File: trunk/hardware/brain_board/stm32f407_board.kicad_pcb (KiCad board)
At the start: 2 copper layers, 65.8 x 73.2 mm, 63 parts, among them J1 MINI-USB-5P-3400020P1, P1 CONN_25X2, P2 CONN_25X2, P3 CONN_2, P4 CONN_6, SW1 SW_PUSH, SW2 SW_PUSH, U1 STM32F407VG, U2 USBUF02W6, U3 LM2937, X1 CRYSTAL

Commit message: improved version
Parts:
- moved C1 14.2 mm to (130.6, 121.9), turned to 270 degrees
- moved C10 11.0 mm to (101.2, 95.0), turned to 180 degrees
- moved C9 8.27 mm to (128.5, 93.6)
- moved R11 5.69 mm to (120.8, 87.1), turned to 90 degrees
- moved C7 5.62 mm to (104.0, 101.1)
- moved D6 5.59 mm to (132.2, 148.7)
- moved FB1 5.36 mm to (101.1, 96.9)
- moved C11 4.95 mm to (112.1, 95.5)
- moved R3 4.13 mm to (120.1, 132.7), turned to 0 degrees
- moved R12 3.78 mm to (129.2, 149.5), turned to 90 degrees
- moved R10 3.72 mm to (104.9, 103.8)
- moved R4 3.32 mm to (132.2, 107.6)
- moved R1 3.28 mm to (117.0, 126.0), turned to 0 degrees
- moved C15 3.14 mm to (106.9, 121.8)
- moved R14 2.92 mm to (126.2, 154.8)
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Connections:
- C7 pad 2: N-0000046 -> N-00000118
- C8 pad 2: N-00000119 -> N-00000118
- FB1 pad 1: N-0000046 -> N-00000118
- R10 pad 1: N-0000046 -> N-00000118
- U1 pad 22: N-0000046 -> N-00000118
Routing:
- net GND: track 122.7 -> 421.1 mm, vias 28 -> 21
- net /VDD: track 323.6 -> 260.4 mm, vias 4 -> 7
- net /PA13: track 149.9 -> 91.8 mm, vias 0 -> 1
- net /PA14: track 134.9 -> 88.4 mm, vias 0 -> 2
- net /NRST: track 89.2 -> 114.5 mm
- net N-00000118: track 0.00 -> 21.2 mm
- net N-0000045: track 67.8 -> 49.1 mm
- net /PA12: track 25.6 -> 44.1 mm
- net /PE6: track 39.7 -> 22.6 mm
- net /PC9: track 43.3 -> 58.6 mm
- net /BOOT0: track 21.2 -> 35.9 mm, vias 0 -> 1
- net /PC7: track 46.9 -> 60.5 mm
- net /PD14: track 44.8 -> 57.5 mm
- net N-0000046: track 12.0 -> 0.00 mm
- net N-0000017: track 23.6 -> 13.1 mm
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
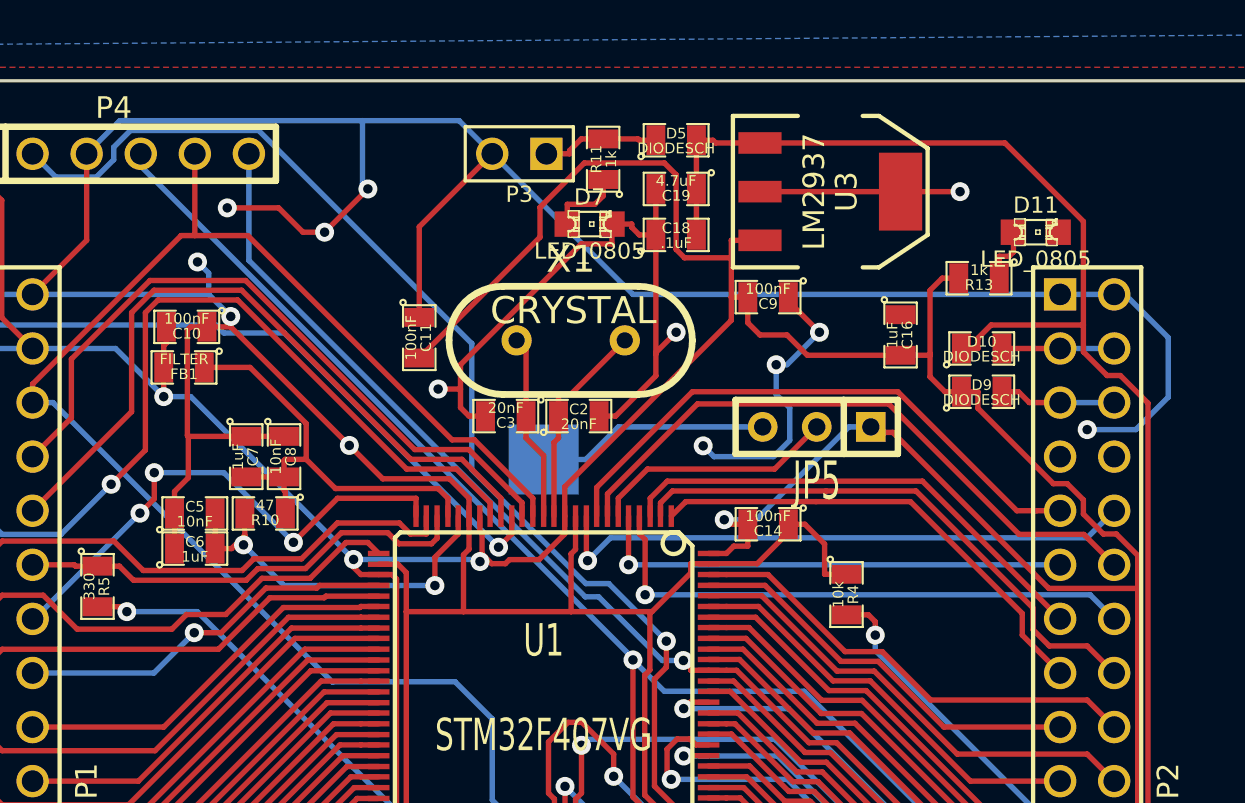
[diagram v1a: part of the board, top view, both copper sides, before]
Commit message: with RTC crystal
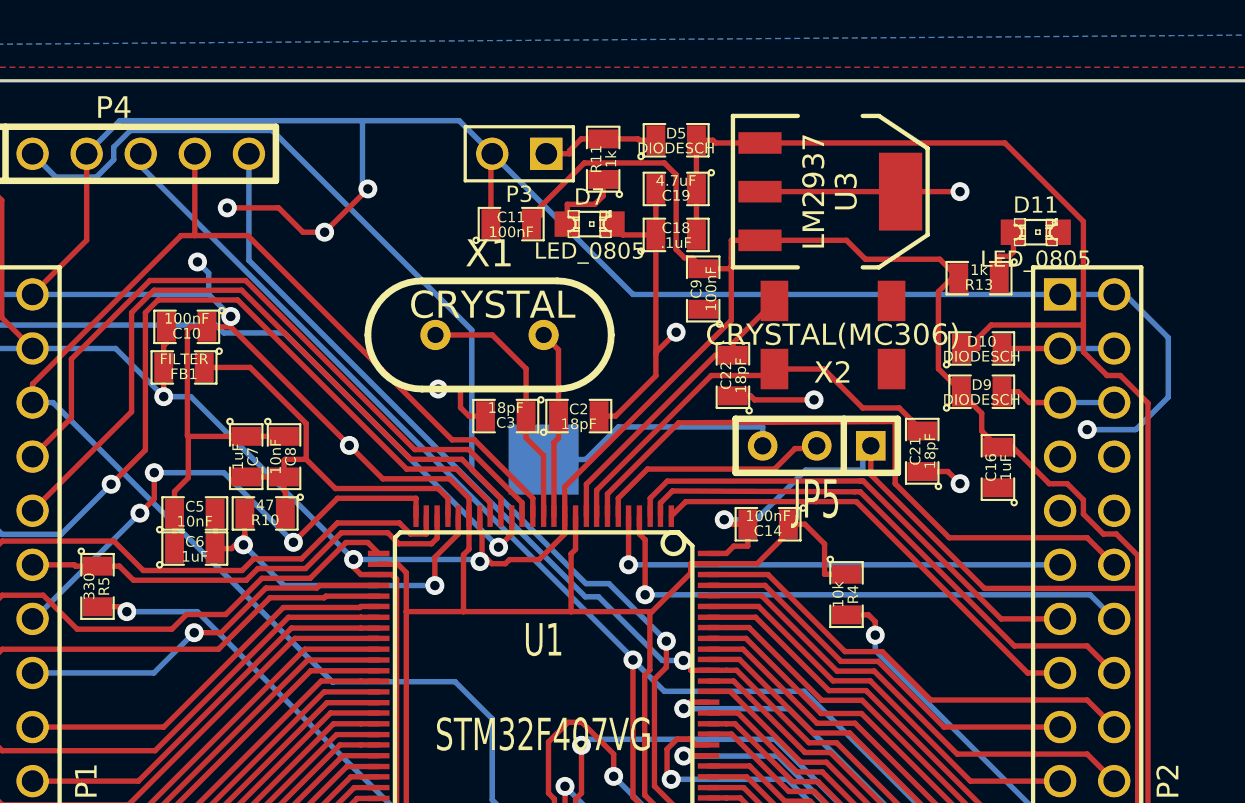
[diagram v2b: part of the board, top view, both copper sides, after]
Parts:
- added C21: 18pF, SM0805, F.Cu at (135.8, 100.8)
- added C22: 18pF, SM0805, F.Cu at (126.9, 97.3)
- added X2: CRYSTAL(MC306), MC-306, F.Cu at (131.6, 95.4)
- C2, C3: value 20nF -> 18pF
- moved C16 7.72 mm to (139.3, 101.6), turned to 90 degrees
- moved C11 6.86 mm to (116.5, 90.2), turned to 0 degrees
- moved X1 3.82 mm to (115.4, 95.4)
- moved C9 3.07 mm to (125.5, 93.2), turned to 90 degrees
- moved JP5 0.89 mm to (130.8, 100.6)
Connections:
- P2 pad 10: /PC15 -> N-0000075
- P2 pad 9: /PC14 -> N-0000076
- U1 pad 8: /PC14 -> N-0000073
- U1 pad 9: /PC15 -> N-0000074
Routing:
- net /PC15: track 27.8 -> 0.00 mm, vias 1 -> 0
- net /PC14: track 27.3 -> 0.00 mm
- net GND: track 421.1 -> 396.2 mm, vias 21 -> 20
- net N-0000073: track 0.00 -> 20.1 mm
- net N-0000074: track 0.00 -> 14.4 mm
- net /VDD: track 260.4 -> 250.6 mm
- net N-00000116: track 8.78 -> 12.2 mm
- net N-00000118: track 9.98 -> 8.89 mm
- net /PC13: track 29.7 -> 30.7 mm
- net N-0000045: track 10.9 -> 11.8 mm
- net /PE3: track 26.3 -> 25.7 mm

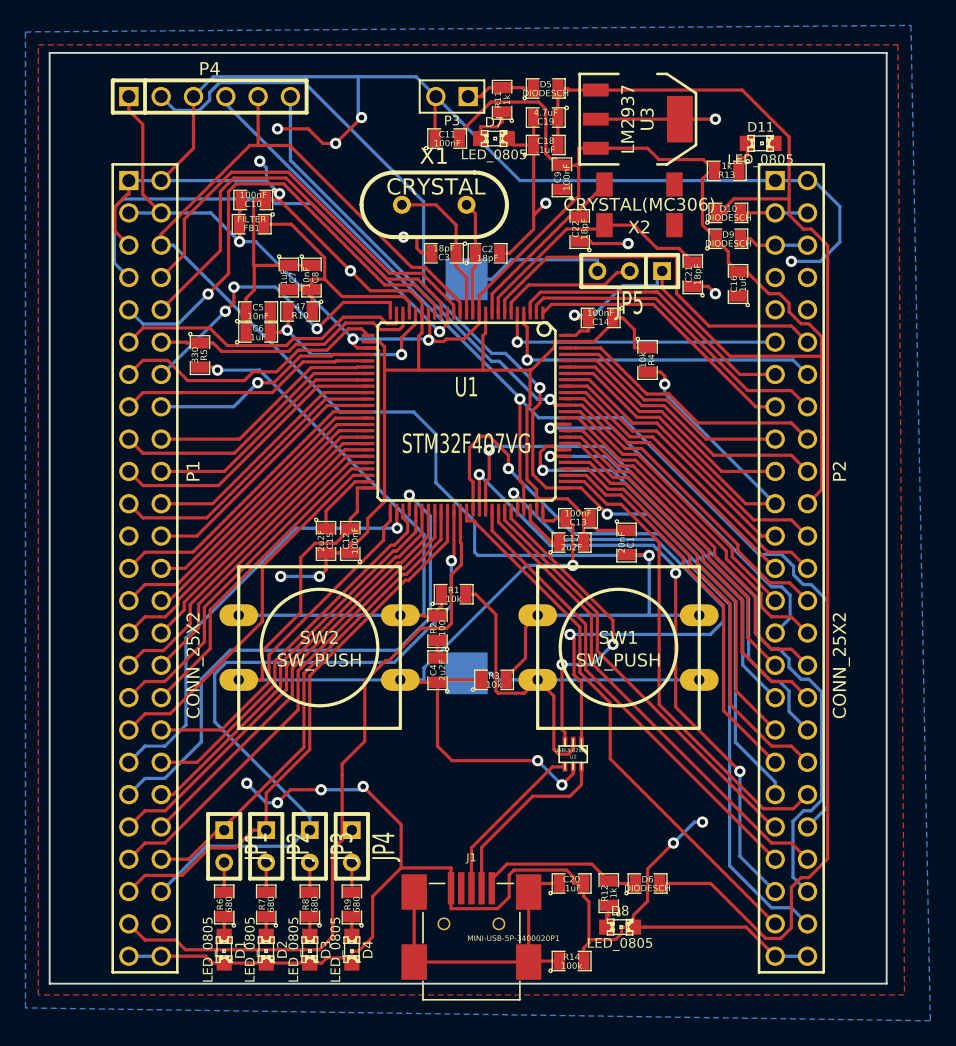
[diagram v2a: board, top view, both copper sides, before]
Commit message: 
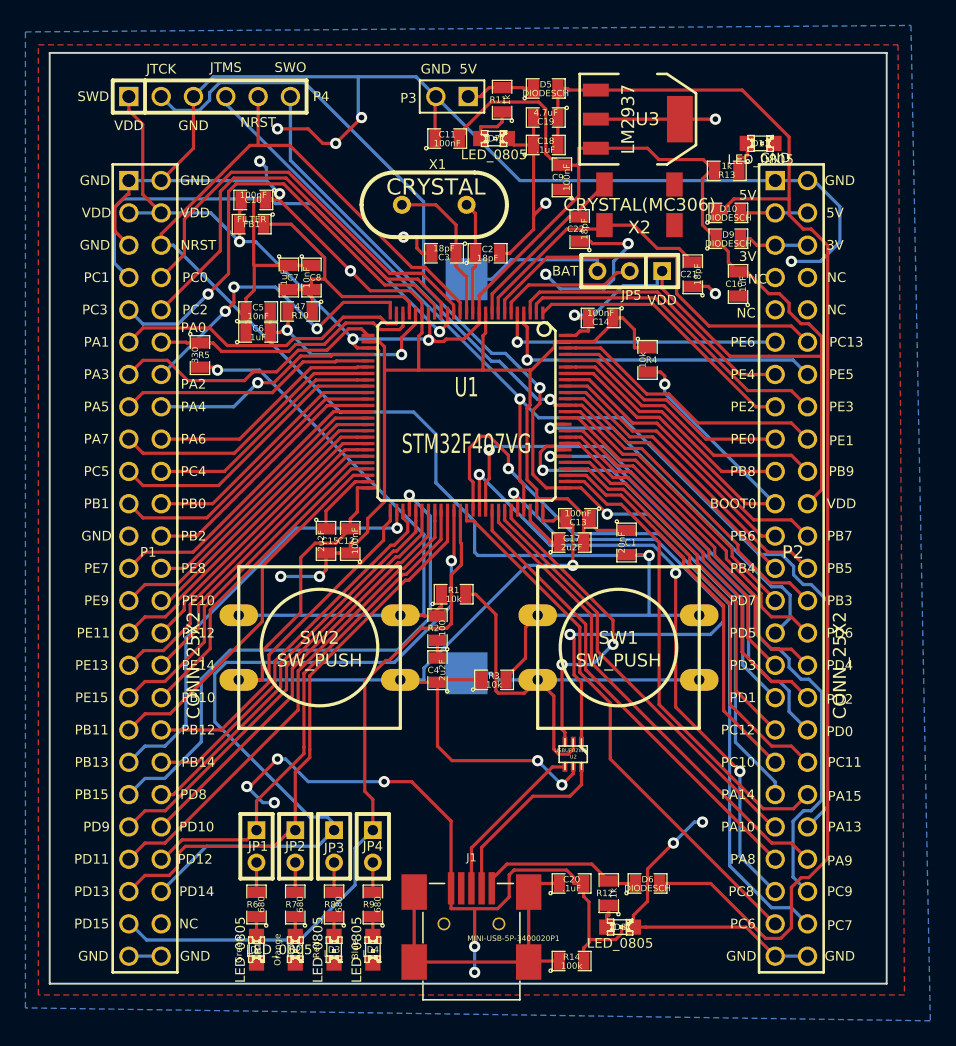
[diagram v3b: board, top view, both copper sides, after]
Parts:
- moved D1 2.54 mm to (101.5, 153.9)
- moved JP1 2.54 mm to (101.5, 145.8)
- moved R6 2.54 mm to (101.5, 150.4)
- moved D2 2.29 mm to (104.5, 153.9)
- moved JP2 2.29 mm to (104.5, 145.8)
- moved R7 2.29 mm to (104.5, 150.4)
- moved D3 1.91 mm to (107.6, 153.9)
- moved JP3 1.91 mm to (107.6, 145.8)
- moved R8 1.91 mm to (107.6, 150.4)
- moved D4 1.65 mm to (110.6, 153.9)
- moved JP4 1.65 mm to (110.6, 145.8)
- moved R9 1.65 mm to (110.6, 150.4)
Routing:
- net GND: track 396.2 -> 389.3 mm, vias 20 -> 23
- net /PD14: track 57.5 -> 61.0 mm
- net /PD15: track 57.4 -> 54.9 mm
- net /PD13: track 44.0 -> 45.9 mm
- net /PD12: track 38.4 -> 39.7 mm
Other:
- board text added: "3V"
- board text added: "5V"
- board text added: "BAT"
- board text added: "BOOT0"
- board text added: "Blue"
- board text added: "GND"
- board text added: "Green"
- board text added: "JTCK"
- board text added: "JTMS"
- board text added: "NC"
- board text added: "NRST"
- board text added: "Orange"
- board text added: "PA0"
- board text added: "PA1"
- board text added: "PA10"
- board text added: "PA13"
- board text added: "PA14"
- board text added: "PA15"
- board text added: "PA2"
- board text added: "PA3"
- board text added: "PA4"
- board text added: "PA5"
- board text added: "PA6"
- board text added: "PA7"
- board text added: "PA8"
- board text added: "PA9"
- board text added: "PB0"
- board text added: "PB1"
- board text added: "PB10"
- board text added: "PB11"
- board text added: "PB12"
- board text added: "PB13"
- board text added: "PB14"
- board text added: "PB15"
- board text added: "PB2"
- board text added: "PB3"
- board text added: "PB4"
- board text added: "PB5"
- board text added: "PB6"
- board text added: "PB7"
- board text added: "PB8"
- board text added: "PB9"
- board text added: "PC0"
- board text added: "PC1"
- board text added: "PC10"
- board text added: "PC11"
- board text added: "PC12"
- board text added: "PC13"
- board text added: "PC2"
- board text added: "PC3"
- board text added: "PC4"
- board text added: "PC5"
- board text added: "PC6"
- board text added: "PC7"
- board text added: "PC8"
- board text added: "PC9"
- board text added: "PD0"
- board text added: "PD1"
- board text added: "PD10"
- board text added: "PD11"
- board text added: "PD12"
- board text added: "PD13"
- board text added: "PD14"
- board text added: "PD15"
- board text added: "PD2"
- board text added: "PD3"
- board text added: "PD4"
- board text added: "PD5"
- board text added: "PD6"
- board text added: "PD7"
- board text added: "PD8"
- board text added: "PD9"
- board text added: "PE0"
- board text added: "PE1"
- board text added: "PE10"
- board text added: "PE11"
- board text added: "PE12"
- board text added: "PE13"
- board text added: "PE14"
- board text added: "PE15"
- board text added: "PE2"
- board text added: "PE3"
- board text added: "PE4"
- board text added: "PE5"
- board text added: "PE6"
- board text added: "PE7"
- board text added: "PE8"
- board text added: "PE9"
- board text added: "Red"
- board text added: "SWD"
- board text added: "SWO"
- board text added: "VDD"

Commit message: size reduction better silkscreen
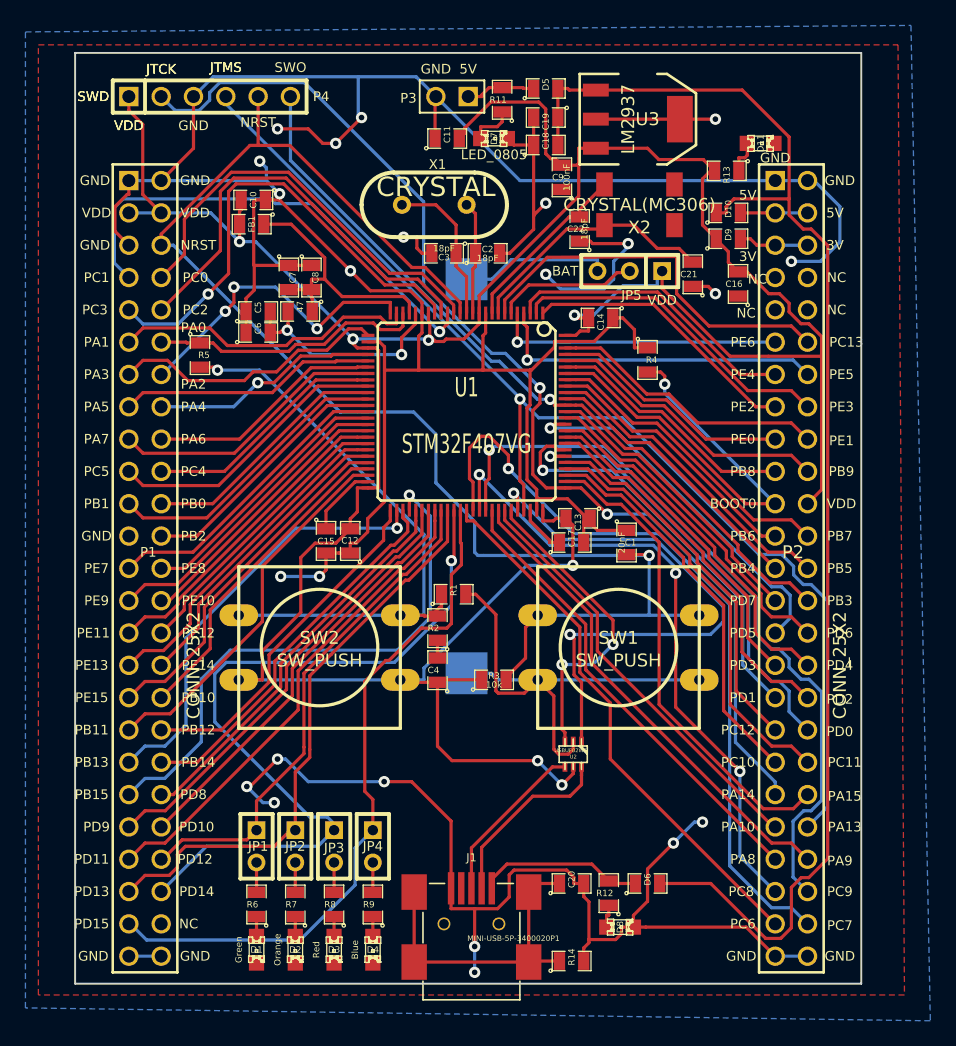
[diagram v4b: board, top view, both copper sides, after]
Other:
- board size 65.8 x 73.2 mm -> 61.8 x 73.2 mm

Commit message: 
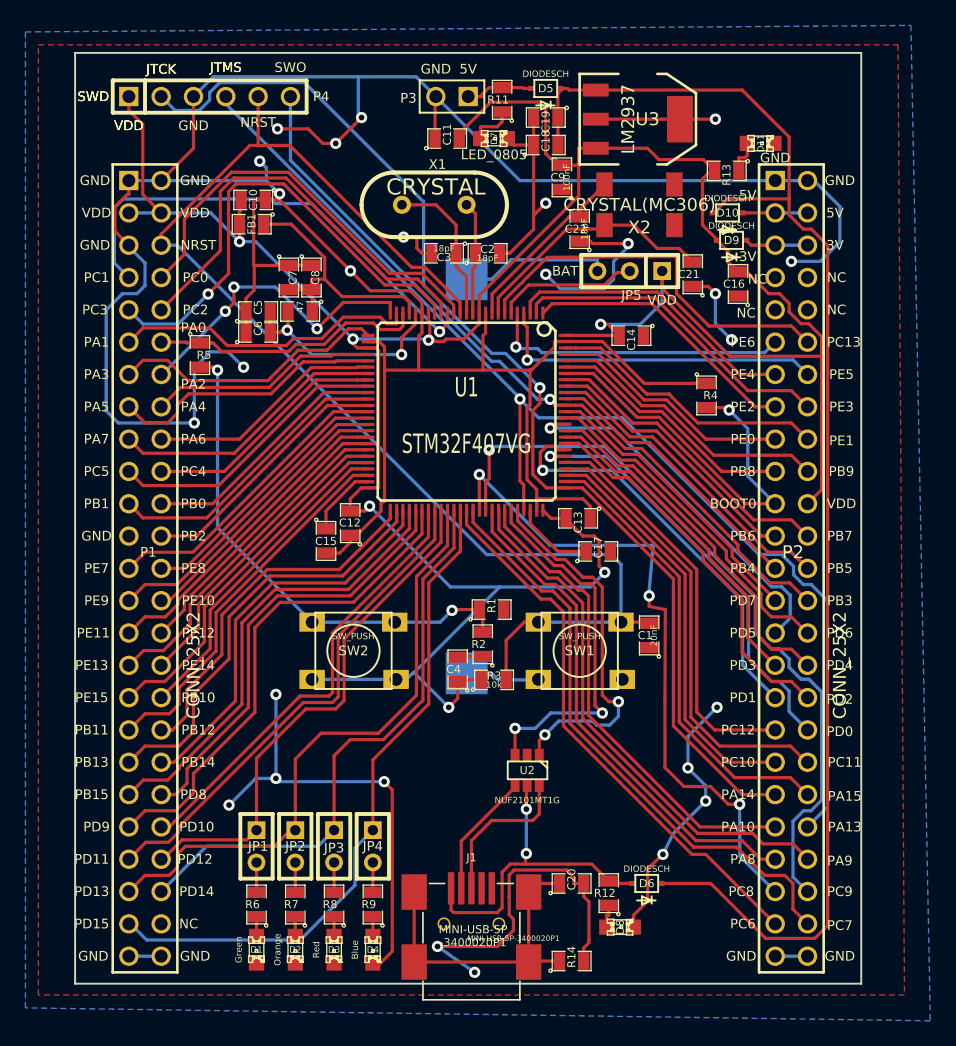
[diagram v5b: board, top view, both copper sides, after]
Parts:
- added G1: LOGO, LOGO_F, B.Cu at (116.8, 139.4)
- D10, D5, D6, D9: footprint SM0805 -> SOD-323
- SW1, SW2: footprint SW_PUSH-12mm -> TL-1105
- U2: value USBUF02W6 -> NUF2101MT1G; footprint sot323-6 -> SOT-457
- moved C1 7.52 mm to (132.3, 129.2), turned to 90 degrees
- moved R4 5.41 mm to (136.8, 110.4)
- moved U2 3.84 mm to (122.7, 139.8)
- moved R2 3.78 mm to (119.3, 129.9)
- moved R1 3.22 mm to (120.0, 127.2)
- moved SW1 3.06 mm to (126.9, 130.4)
- moved C14 2.79 mm to (130.9, 105.7)
- moved SW2 2.68 mm to (109.1, 130.4)
- moved C17 2.21 mm to (128.3, 122.6)
- moved C4 1.59 mm to (117.3, 131.9)
- moved C12 1.40 mm to (108.8, 120.4)
- moved D9 0.28 mm to (138.8, 98.2)
- moved D6 0.06 mm to (132.1, 148.7)
- moved D10 0.06 mm to (138.5, 96.0)
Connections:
- D6 pad 1: N-0000023 -> /Vbus
- J1 pad 1: N-0000023 -> /Vbus
- J1 pad 2: N-0000059 (its old number) -> /D-
- J1 pad 3: N-0000060 -> /D+
- R12 pad 2: N-0000023 -> /Vbus
- U2 pad 4: N-0000060 -> /D-
- U2 pad 5: /VDD -> /Vbus
- U2 pad 6: N-0000059 (its old number) -> /D+
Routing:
- net /Vbus: track 0.00 -> 26.3 mm, vias 0 -> 2
- net /VDD: track 250.6 -> 228.3 mm
- net N-0000059 (its old number): track 15.2 -> 0.00 mm
- net /PD14: track 61.0 -> 46.2 mm, vias 1 -> 0
- net /PA12: track 44.1 -> 29.3 mm
- net /PC7: track 60.5 -> 46.8 mm, vias 1 -> 0
- net N-0000060: track 13.2 -> 0.00 mm
- net N-0000023: track 13.1 -> 0.00 mm
- net /D+: track 0.00 -> 12.0 mm
- net /NRST: track 114.5 -> 103.1 mm, vias 1 -> 0
- net /D-: track 0.00 -> 9.70 mm
- net N-0000049: track 49.1 -> 39.8 mm, vias 1 -> 2
- net /PB15: track 43.8 -> 36.0 mm, vias 1 -> 0
- net /PA11: track 24.7 -> 29.3 mm
- net /BOOT0: track 35.9 -> 31.5 mm
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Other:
- board text added: "MINI-USB-5P -3400020P1"
